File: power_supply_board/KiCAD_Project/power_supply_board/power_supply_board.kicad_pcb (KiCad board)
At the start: 4 copper layers, 63.5 x 33 mm, 8 parts, among them J1 To Digitiziers, J2 Power Input, U1 TDN 5-2411WI, U2 TDN 5-2422WI

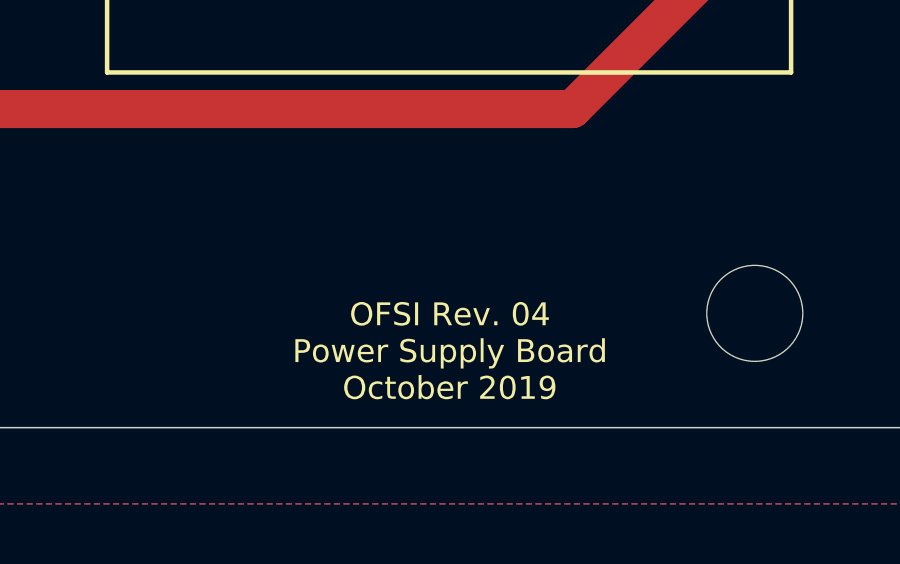
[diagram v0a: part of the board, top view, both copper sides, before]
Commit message: Change power supply to OFMI
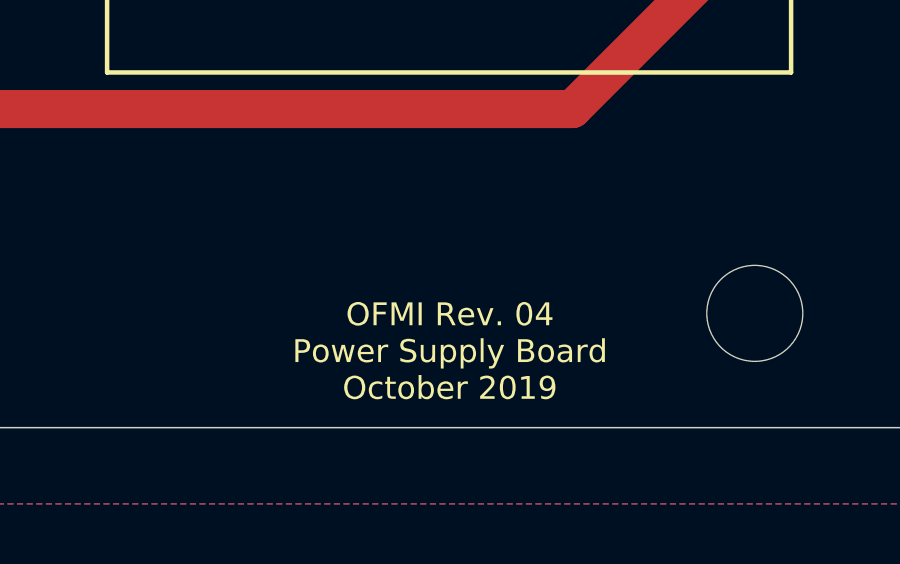
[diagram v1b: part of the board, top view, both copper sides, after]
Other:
- board text added: "OFMI Rev. 04 Power Supply Board October 2019"
- board text removed: "OFSI Rev. 04 Power Supply Board October 2019"
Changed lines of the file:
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@@
     (effects (font (size 0.762 0.762) (thickness 0.14986)) (justify mirror))
   )
-  (gr_text "OFSI Rev. 04\nPower Supply Board\nOctober 2019" (at 171.45 129.54) (layer F.SilkS)
+  (gr_text "OFMI Rev. 04\nPower Supply Board\nOctober 2019" (at 171.45 129.54) (layer F.SilkS)
     (effects (font (size 0.762 0.762) (thickness 0.14986)))
   )

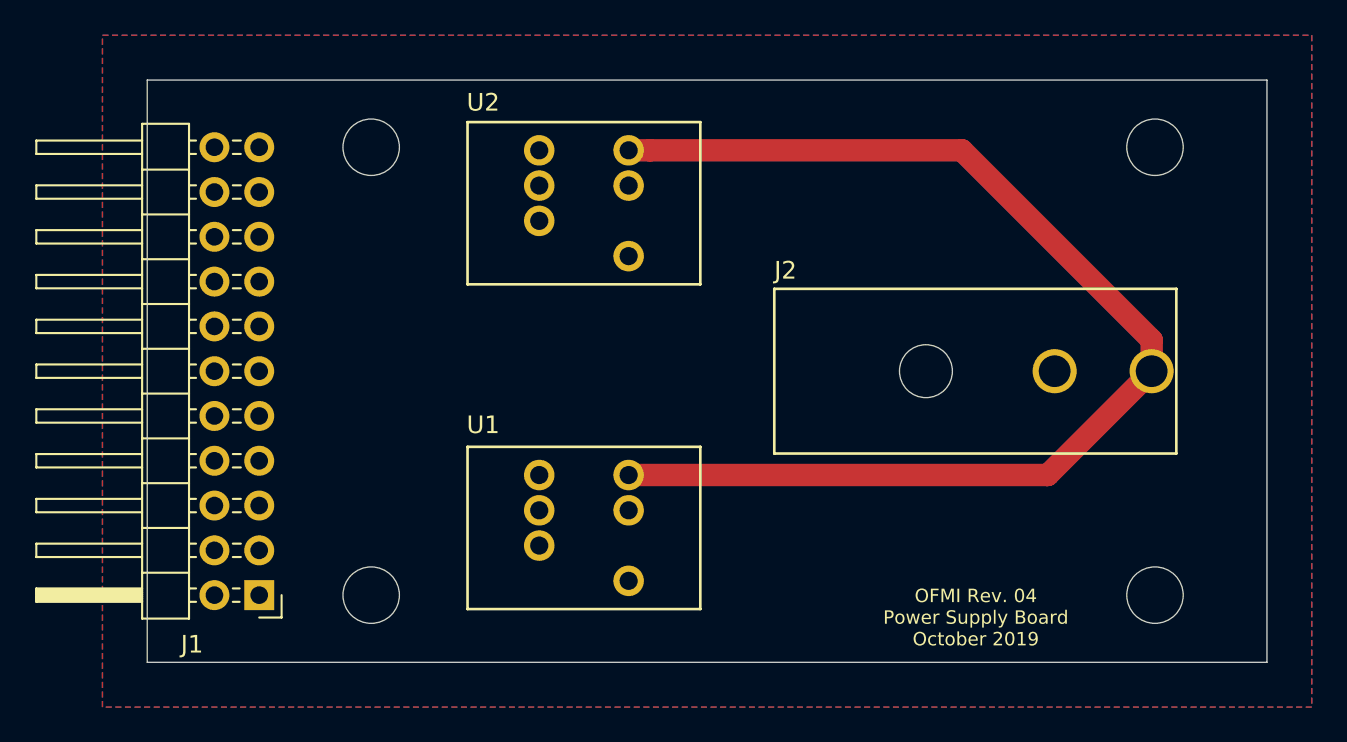
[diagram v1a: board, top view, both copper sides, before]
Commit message: Minor design changes for Rev 4.1. Closes #4, #5, #6.
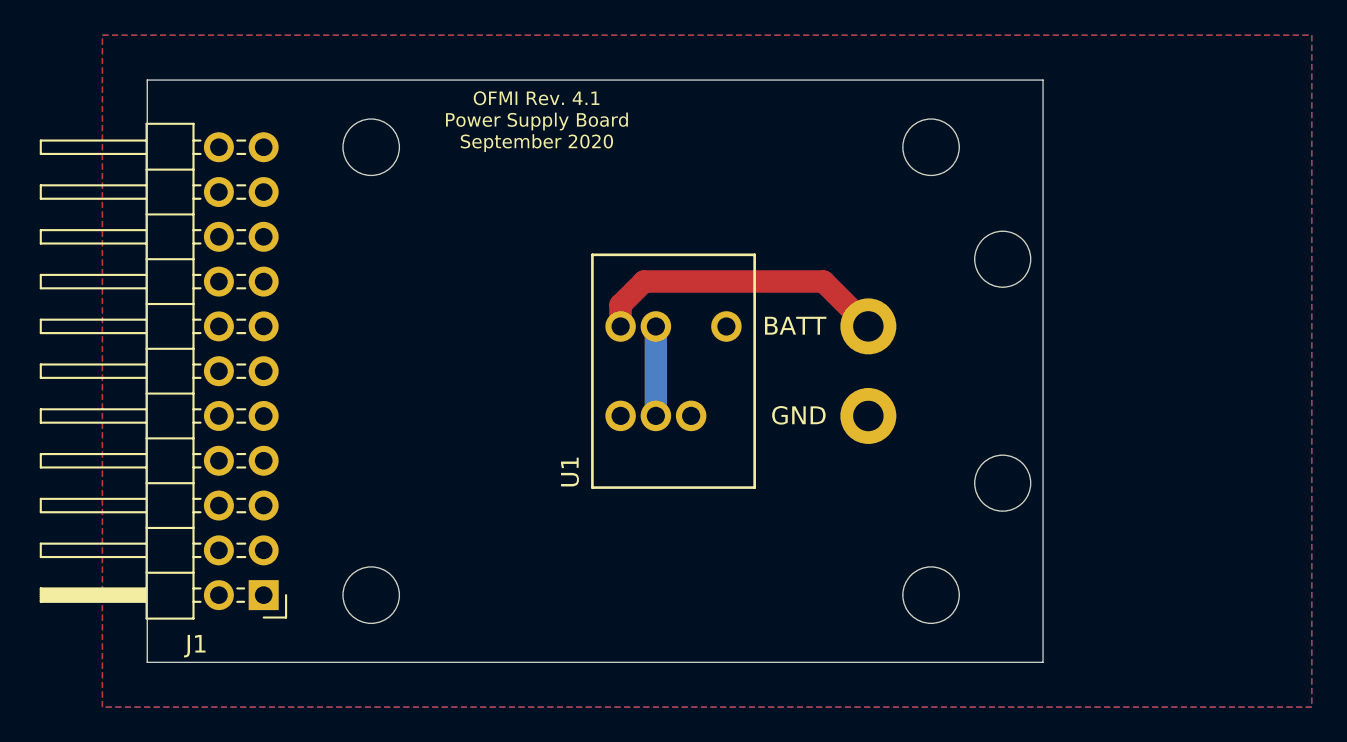
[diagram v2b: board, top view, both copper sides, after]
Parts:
- removed U2: TDN 5-2422WI, lib_fp:TDN5WI
- J2: footprint lib_fp:76825-0002 -> lib_fp:16AWG
- moved H2 12.7 mm to (168.9, 102.9)
- moved H3 12.7 mm to (168.9, 128.3)
- moved U1 10.2 mm to (154.3, 115.6), turned to 270 degrees
- moved J2 5.33 mm to (165.4, 115.6), turned to 0 degrees
- moved J1 0.25 mm to (131.1, 128.3)
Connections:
- J1 pad 3: +12V -> (no net)
- J1 pad 5: -12V -> (no net)
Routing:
- net +BATT: track 68.0 -> 16.9 mm
- net GND: track 0.00 -> 5.07 mm
- added copper zone on F.Cu, net +5V
- added copper zone on B.Cu, net GND
- removed copper zone on In1.Cu, net +12V
- removed copper zone on In2.Cu, net +5V
- removed copper zone on B.Cu, net -12V
- removed copper zone on F.Cu, net GND
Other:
- board size 63.5 x 33 mm -> 50.8 x 33 mm
- copper layers 4 -> 2
- board text added: "BATT"
- board text added: "CS"
- board text added: "LG 3-0000044"
- board text added: "MISO1"
- board text added: "MISO2"
- board text added: "MISO3"
- board text added: "MISO4"
- board text added: "MISO5"
- board text added: "MISO6"
- board text added: "MISO7"
- board text added: "MISO8"
- board text added: "MISO9"
- board text added: "OFMI Rev. 4.1 Power Supply Board September 2020"
- board text removed: "+12"
- board text removed: "-12"
- board text removed: "CS1"
- board text removed: "CS2"
- board text removed: "CS3"
- board text removed: "CS4"
- board text removed: "CS5"
- board text removed: "CS6"
- board text removed: "CS7"
- board text removed: "CS8"
- board text removed: "CS9"
- board text removed: "LG 3-0000016"
- board text removed: "MISO"
- board text removed: "OFMI Rev. 04 Power Supply Board October 2019"
